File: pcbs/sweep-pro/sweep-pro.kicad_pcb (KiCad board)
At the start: 2 copper layers, 115 x 86.7 mm, 50 parts, among them SW1 SW_PUSH-kbd, SW10 SW_PUSH-kbd, SW11 SW_PUSH-kbd, SW12 SW_PUSH-kbd, SW13 SW_PUSH-kbd, SW14 SW_PUSH-kbd, SW15 SW_PUSH-kbd, SW16 SW_PUSH-kbd, SW17 SW_PUSH-kbd, SW2 SW_PUSH-kbd, SW3 SW_PUSH-kbd, SW4 SW_PUSH-kbd, SW5 SW_PUSH-kbd, SW6 SW_PUSH-kbd, SW7 SW_PUSH-kbd, SW8 SW_PUSH-kbd, SW9 SW_PUSH-kbd, U1 ProMicro-kbd

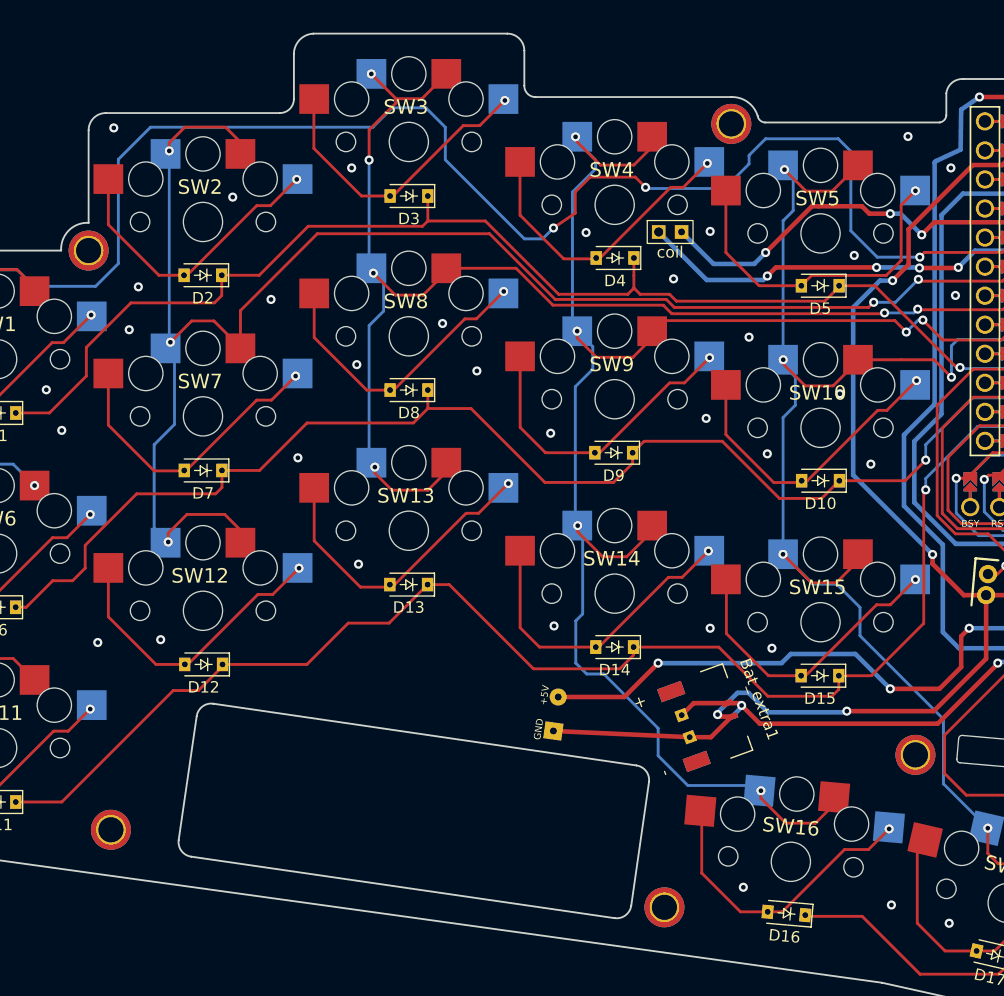
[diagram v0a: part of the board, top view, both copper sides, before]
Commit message: change mouting hole diameter to 3.2mm
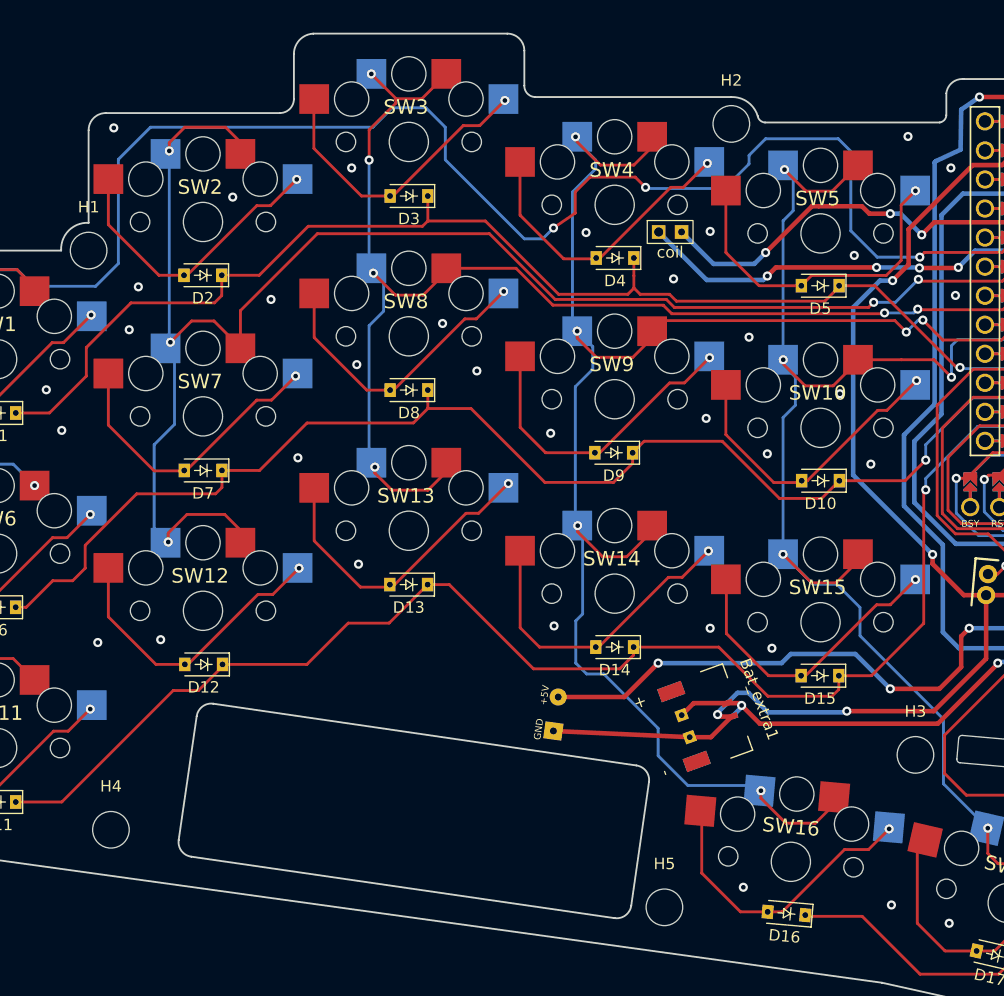
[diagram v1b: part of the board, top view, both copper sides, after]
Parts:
- H1, H2, H3, H4, H5: footprint MountingHole:MountingHole_2.2mm_M2_ISO7380_Pad_TopBottom -> MountingHole:MountingHole_3.2mm_M3_DIN965
